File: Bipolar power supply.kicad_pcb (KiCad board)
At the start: 2 copper layers, 152 x 46 mm, 30 parts, among them J1 Screw 6-32, J2 Screw 6-32, J3 Screw 6-32, J4 Conn_01x03, U1 LM317_TO-220, U2 LM337_TO-220

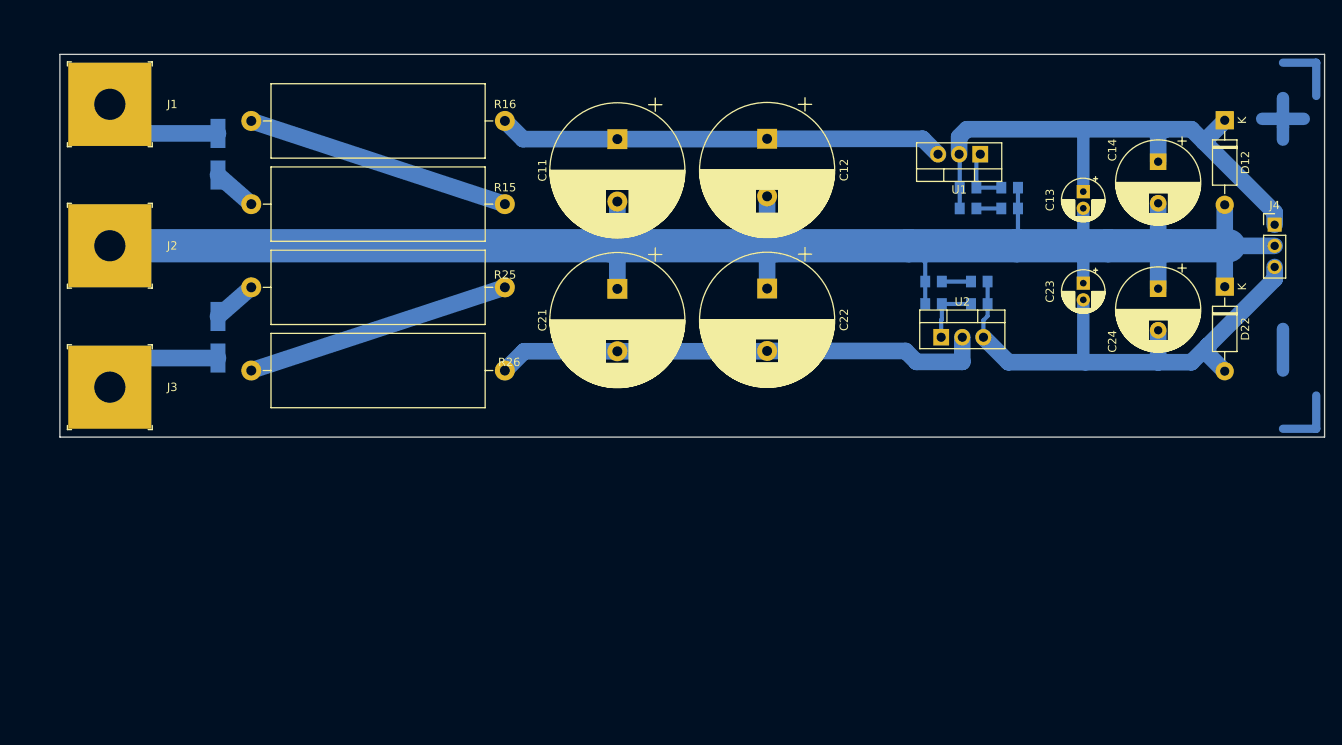
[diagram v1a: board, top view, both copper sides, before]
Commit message: First pass at routing in 70x100 mm panel.
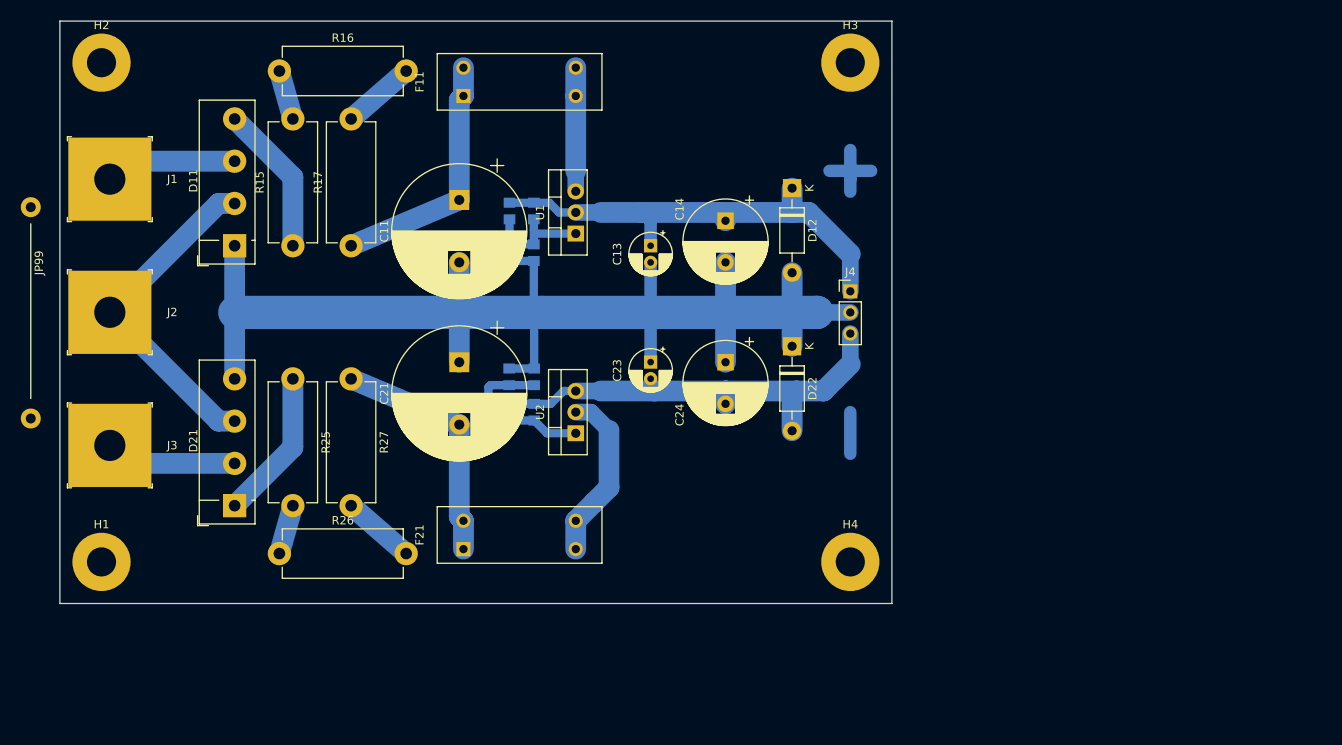
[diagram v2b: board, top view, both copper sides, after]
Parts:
- removed C12, C22: 2200uF, Capacitor_THT:CP_Radial_D16.0mm_P7.50mm
- added F11: Fuse Holder, $Local:FuseHolder_6.8x19.8mm_P3.4x13.5mm_Vetical, F.Cu at (105.2, 57.3)
- added F21: Fuse Holder, $Local:FuseHolder_6.8x19.8mm_P3.4x13.5mm_Vetical, F.Cu at (105.2, 111.8)
- added H1: MountingHole, MountingHole:MountingHole_3.5mm_Pad, F.Cu at (55.0, 115.0)
- added H2: MountingHole, MountingHole:MountingHole_3.5mm_Pad, F.Cu at (55.0, 55.0)
- added H3: MountingHole, MountingHole:MountingHole_3.5mm_Pad, F.Cu at (145.0, 55.0)
- added H4: MountingHole, MountingHole:MountingHole_3.5mm_Pad, F.Cu at (145.0, 115.0)
- added JP99: Open, $Local:Jumper_P25.40mm, F.Cu at (46.5, 72.4)
- added R17: 5, Resistor_THT:R_Axial_DIN0614_L14.3mm_D5.7mm_P15.24mm_Horizontal, F.Cu at (85.0, 77.0)
- added R27: 5, Resistor_THT:R_Axial_DIN0614_L14.3mm_D5.7mm_P15.24mm_Horizontal, F.Cu at (85.0, 93.0)
- D11, D21: value SK310A -> KBL06; footprint Diode_SMD:D_SMA_Handsoldering -> Diode_THT:Diode_Bridge_Vishay_KBL; moved to F.Cu
- R15, R16, R25, R26: footprint $Local:R_Axial_L25.5mm_D8.7mm_P30.48mm_Horizontal -> Resistor_THT:R_Axial_DIN0614_L14.3mm_D5.7mm_P15.24mm_Horizontal
- moved R14 60.3 mm to (104.0, 77.8), turned to -90 degrees
- moved R23 58.6 mm to (104.0, 97.0), turned to 90 degrees
- moved R12 57.7 mm to (107.0, 77.8), turned to -90 degrees
- moved R13 55.1 mm to (104.0, 72.8), turned to -90 degrees
- moved R21 55.1 mm to (107.0, 97.0), turned to 90 degrees
- moved C23 52.9 mm to (121.0, 91.0)
- moved C24 52.7 mm to (130.0, 91.0)
- moved D12 52.6 mm to (138.0, 70.1)
- moved D22 52.5 mm to (138.0, 89.1)
- moved C14 52.5 mm to (130.0, 74.0)
- moved C13 52.4 mm to (121.0, 77.0)
- moved R24 52.3 mm to (104.0, 92.8), turned to -90 degrees
- moved R11 52.3 mm to (107.0, 72.8), turned to -90 degrees
- moved J4 51.6 mm to (145.0, 82.5)
- moved U1 49.5 mm to (112.0, 75.5), turned to 90 degrees
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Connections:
- C11 pad 1: /IN_P -> Net-(C11-Pad1)
- C21 pad 2: /IN_N -> Net-(C21-Pad2)
- D11 pad 1: Net-(D11-Pad1) -> /GND
- D11 pad 2: /AC_P -> /CT
- D21 pad 1: /AC_N -> Net-(D21-Pad1)
- D21 pad 2: Net-(D21-Pad2) -> /AC_N
- J2 pad 1: /GND -> /CT
- R13 pad 2: Net-(R13-Pad2) -> /ADJ_P
- R14 pad 1: Net-(R13-Pad2) -> /ADJ_P
- R15 pad 1: Net-(D11-Pad1) -> Net-(D11-Pad4)
- R16 pad 2: /IN_P -> Net-(R16-Pad2)
- R23 pad 1: Net-(R23-Pad1) -> /ADJ_N
- R24 pad 2: Net-(R23-Pad1) -> /ADJ_N
- R25 pad 1: Net-(D21-Pad2) -> Net-(D21-Pad1)
- R26 pad 2: /IN_N -> Net-(R26-Pad2)
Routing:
- net /GND: track 208.6 -> 160.2 mm
- net /CT: track 0.00 -> 40.8 mm
- net /IN_P: track 53.7 -> 14.9 mm
- net /IN_N: track 59.5 -> 20.8 mm
- net Net-(C11-Pad1): track 0.00 -> 30.2 mm
- net Net-(C21-Pad2): track 0.00 -> 29.3 mm
- net Net-(R15-Pad2): track 32.1 -> 5.98 mm
- net Net-(R25-Pad2): track 32.1 -> 5.98 mm
- net Net-(D11-Pad4): track 0.00 -> 18.1 mm
- net Net-(D21-Pad1): track 0.00 -> 18.1 mm
- net (no net): track 31.0 -> 15.0 mm
- net /ADJ_N: track 7.53 -> 20.4 mm
- net /VPOS: track 67.6 -> 56.5 mm
- net /VNEG: track 64.1 -> 54.9 mm
- net Net-(R26-Pad2): track 0.00 -> 8.78 mm
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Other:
- board size 152 x 46 mm -> 100 x 70 mm

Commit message: Created footprint for TO-220 with Heatsink
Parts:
- U1, U2: footprint Package_TO_SOT_THT:TO-220-3_Vertical -> $Local:TO-220-3_Vertical_Heatsink_19.1x9.7mm

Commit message: Routing WIP.
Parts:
- removed R11, R13, R21, R23: 249, $Local:R_0805_2012Metric_Pad1.20x1.40mm_HandSolder
- removed R12, R14, R22, R24: 2.73K, $Local:R_0805_2012Metric_Pad1.20x1.40mm_HandSolder
- moved R25 39.6 mm to (64.0, 130.0), turned to 0 degrees
- moved R27 39.5 mm to (98.7, 130.0), turned to 180 degrees
- moved R16 21.7 mm to (83.5, 76.5)
- moved D11 19.2 mm to (73.0, 96.1)
- moved F21 18.2 mm to (112.8, 128.3)
- moved C21 17.1 mm to (91.0, 106.6)
- moved F11 16.1 mm to (106.0, 73.4)
- moved C11 15.9 mm to (91.0, 85.7)
- moved D12 15.8 mm to (138.0, 85.9)
- moved R15 15.7 mm to (64.0, 70.0), turned to 0 degrees
- moved U2 15.6 mm to (110.9, 115.1)
- moved C23 15.5 mm to (121.0, 106.5)
- moved R17 15.4 mm to (98.7, 70.0), turned to 180 degrees
- moved C14 15.0 mm to (130.0, 89.0)
- moved H1 15.0 mm to (55.0, 130.0)
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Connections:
- R17 pad 1: Net-(C11-Pad1) -> Net-(R16-Pad2)
- R17 pad 2: Net-(R16-Pad2) -> Net-(C11-Pad1)
- R27 pad 1: Net-(C21-Pad2) -> Net-(R26-Pad2)
- R27 pad 2: Net-(R26-Pad2) -> Net-(C21-Pad2)
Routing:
- net /GND: track 160.2 -> 134.4 mm
- net /CT: track 40.8 -> 63.1 mm
- net /ADJ_N: track 20.4 -> 0.00 mm
- net /AC_N: track 15.9 -> 36.3 mm
- net /AC_P: track 15.9 -> 35.6 mm
- net Net-(C21-Pad2): track 29.3 -> 46.7 mm
- net Net-(C11-Pad1): track 30.2 -> 46.5 mm
- net /VPOS: track 56.5 -> 40.7 mm
- net /ADJ_P: track 13.9 -> 0.00 mm
- net /VNEG: track 54.9 -> 43.9 mm
- net /IN_P: track 14.9 -> 20.3 mm
- net Net-(D21-Pad1): track 18.1 -> 14.0 mm
- net Net-(D11-Pad4): track 18.1 -> 14.1 mm
- net /IN_N: track 20.8 -> 23.2 mm
- net Net-(R15-Pad2): track 5.98 -> 8.26 mm
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
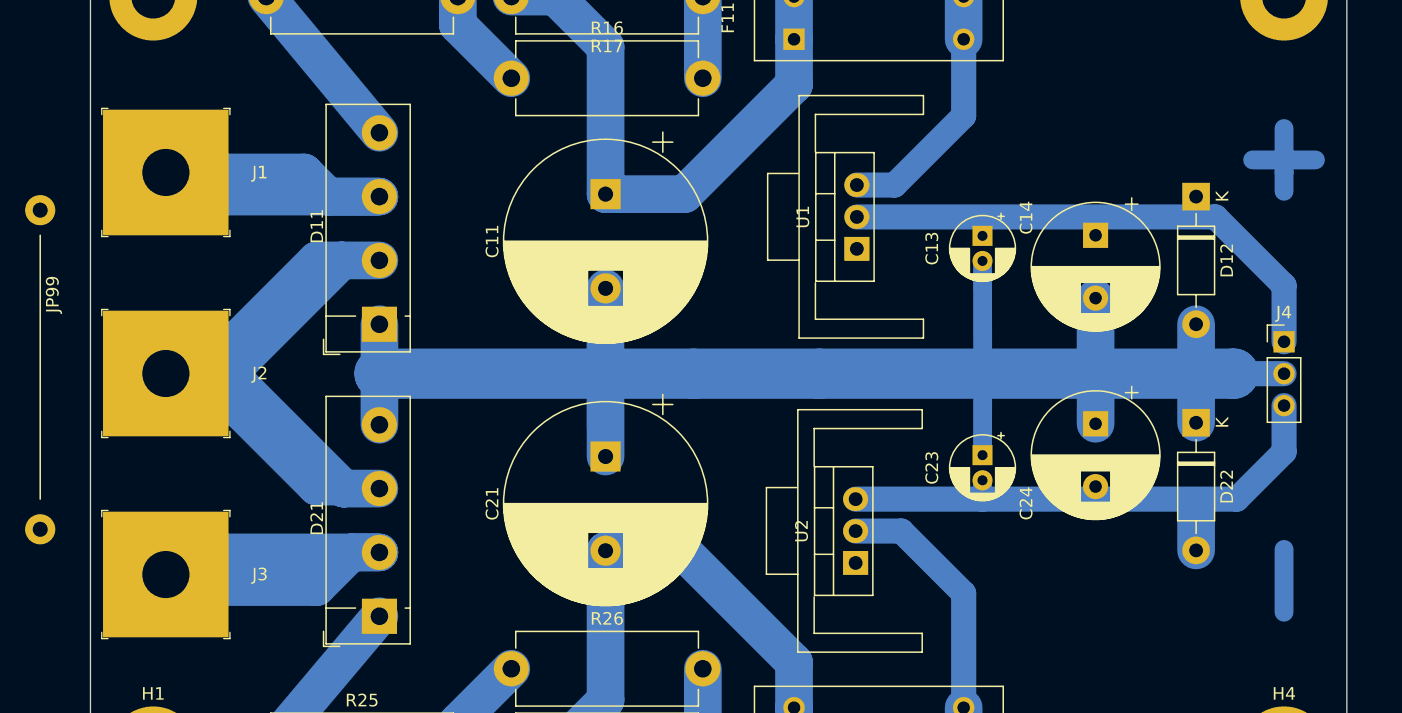
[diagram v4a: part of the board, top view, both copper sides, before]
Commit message: Routing done. Used for dry fit.
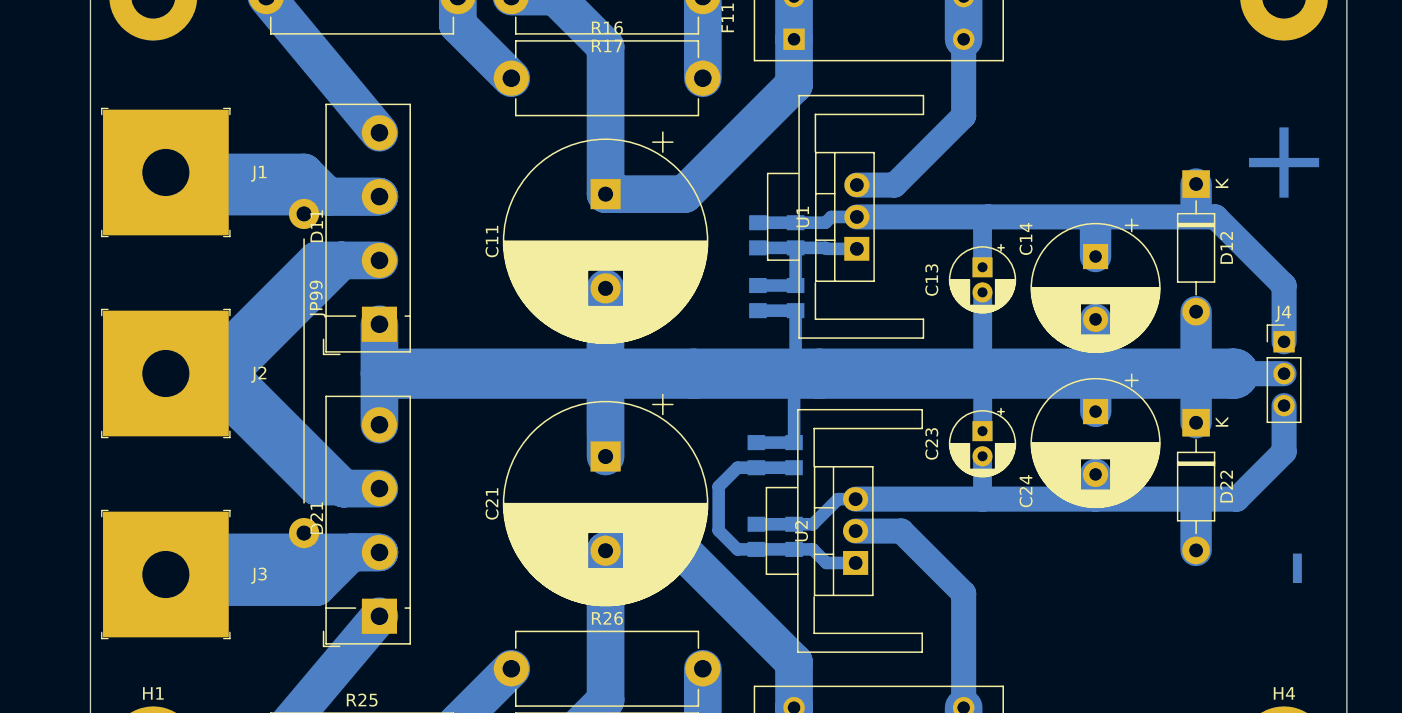
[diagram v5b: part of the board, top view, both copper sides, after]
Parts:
- added R11: 249, $Local:R_0805_2012Metric_Pad1.20x1.40mm_HandSolder, B.Cu at (106.1, 89.0)
- added R12: 2.73K, $Local:R_0805_2012Metric_Pad1.20x1.40mm_HandSolder, B.Cu at (106.1, 94.0)
- added R13: 249, $Local:R_0805_2012Metric_Pad1.20x1.40mm_HandSolder, B.Cu at (103.1, 89.0)
- added R14: 2.73K, $Local:R_0805_2012Metric_Pad1.20x1.40mm_HandSolder, B.Cu at (103.1, 94.0)
- added R21: 249, $Local:R_0805_2012Metric_Pad1.20x1.40mm_HandSolder, B.Cu at (106.0, 113.0)
- added R22: 2.73K, $Local:R_0805_2012Metric_Pad1.20x1.40mm_HandSolder, B.Cu at (106.0, 106.5)
- added R23: 249, $Local:R_0805_2012Metric_Pad1.20x1.40mm_HandSolder, B.Cu at (103.0, 113.0)
- added R24: 2.73K, $Local:R_0805_2012Metric_Pad1.20x1.40mm_HandSolder, B.Cu at (103.0, 106.5)
- moved JP99 21.0 mm to (67.0, 87.3)
- moved C13 2.50 mm to (121.0, 91.5)
- moved C23 1.91 mm to (121.0, 104.6)
- moved C14 1.69 mm to (130.0, 90.7)
- moved D12 1.00 mm to (138.0, 84.9)
- moved C24 0.97 mm to (130.0, 103.0)
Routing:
- net /ADJ_N: track 0.00 -> 22.1 mm
- net /VPOS: track 40.7 -> 56.8 mm
- net (no net): track 15.0 -> 0.00 mm
- net /ADJ_P: track 0.00 -> 13.9 mm
- net /VNEG: track 43.9 -> 55.5 mm
- net /GND: track 134.4 -> 141.3 mm
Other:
- board text added: "+"
- board text added: "-"

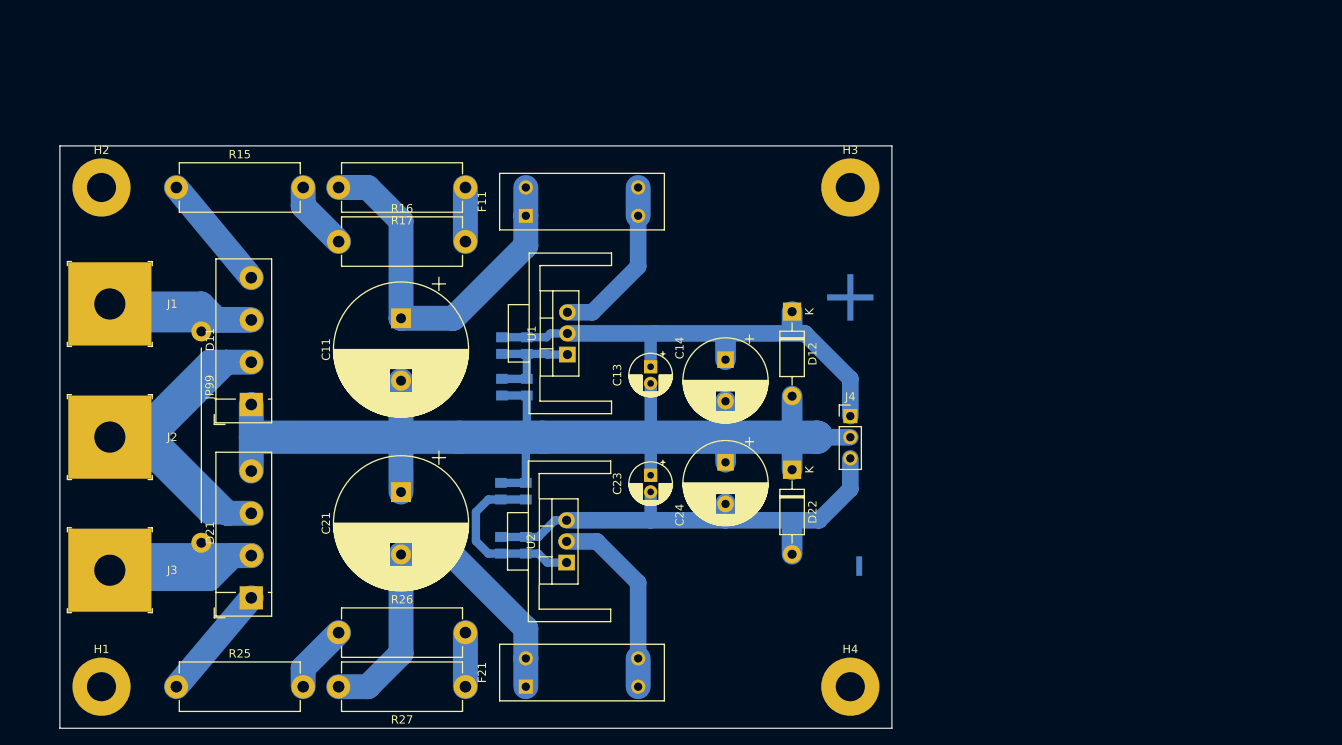
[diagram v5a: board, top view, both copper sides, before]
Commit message: Updated footprints from dry fit.
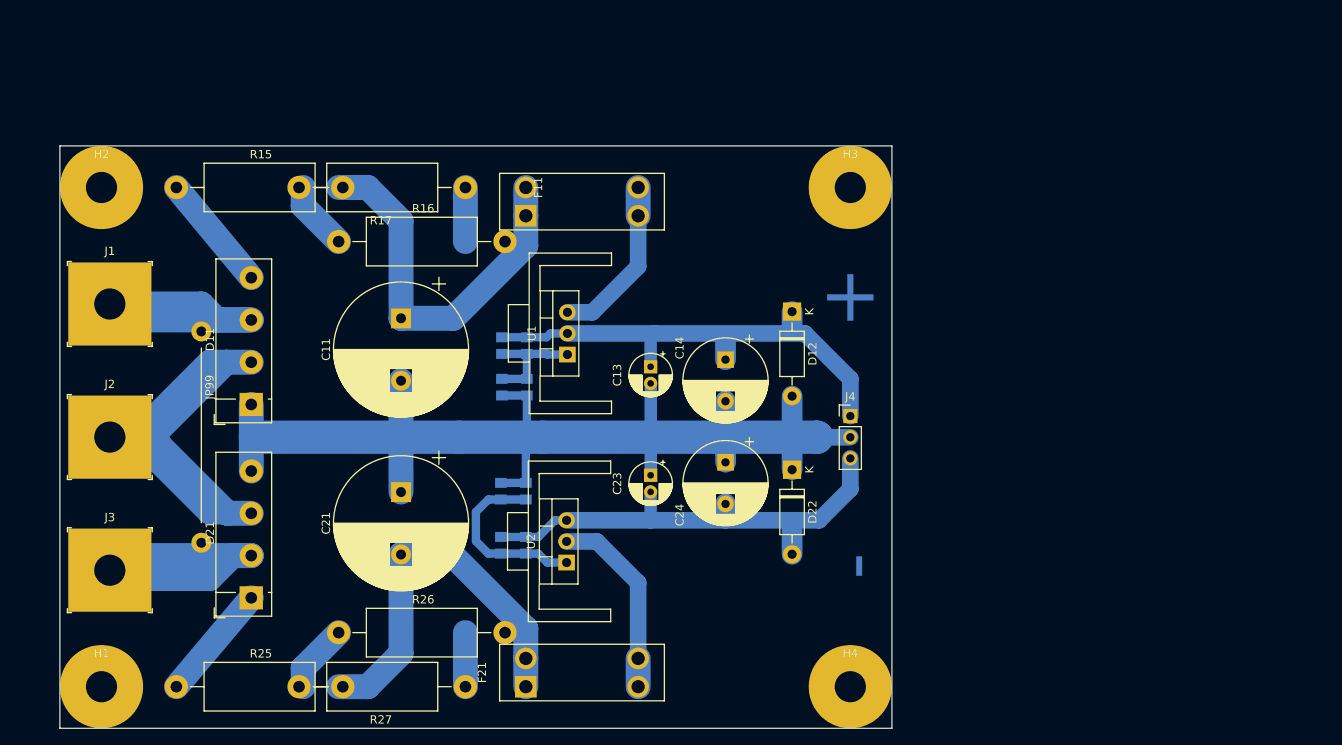
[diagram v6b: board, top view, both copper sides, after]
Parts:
- H1, H2, H3, H4: footprint MountingHole:MountingHole_3.5mm_Pad -> $Local:MountingHole_#6-32_Pad_10mm
- J1, J2, J3: value Screw 6-32 -> Screw #6-32; footprint $Local:ScrewTerminal_01x01_6-32_10mm -> $Local:ScrewTerminal_01x01_#6-32_10mm
- R15, R16, R17, R25, R26, R27: footprint Resistor_THT:R_Axial_DIN0614_L14.3mm_D5.7mm_P15.24mm_Horizontal -> $Local:R_Axial_L13.1mm_D5.6mm_P20.0mm_Horizontal
- moved F11 6.96 mm to (112.8, 71.7)
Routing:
- net Net-(R25-Pad2): track 8.26 -> 0.00 mm
- net Net-(C21-Pad2): track 46.7 -> 55.0 mm
